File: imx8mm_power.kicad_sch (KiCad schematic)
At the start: 58 parts, among them U1 MIMX8MM6DVTLZAA

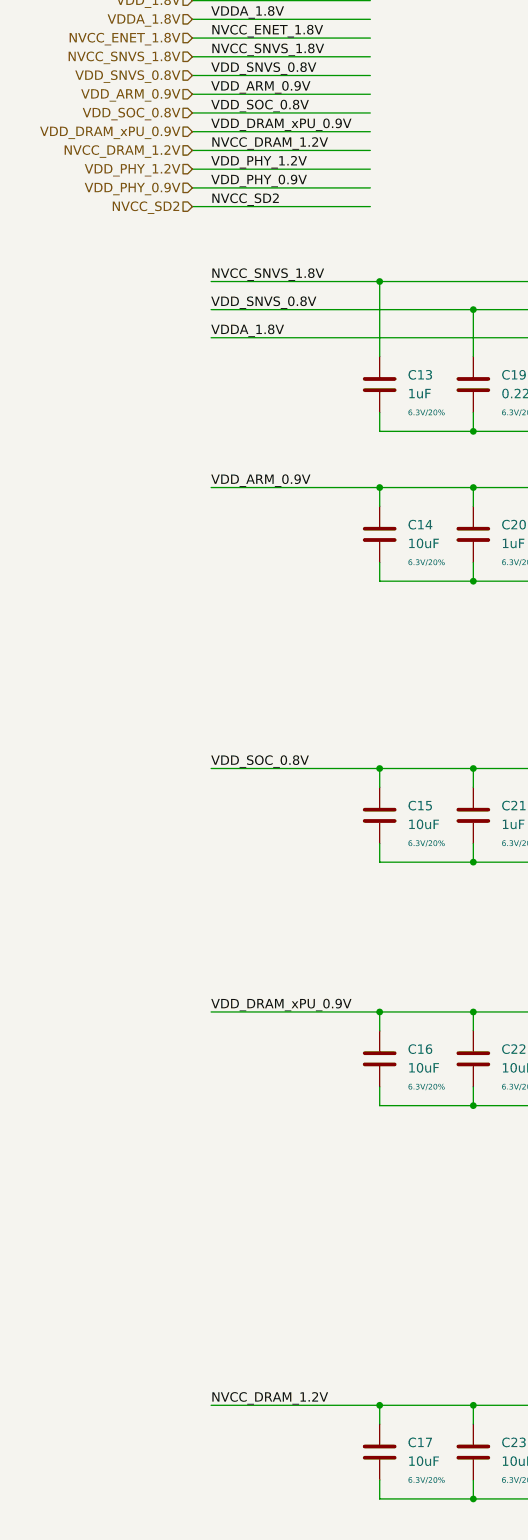
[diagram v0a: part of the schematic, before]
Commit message: add inital ddr tool version, lots of routing work
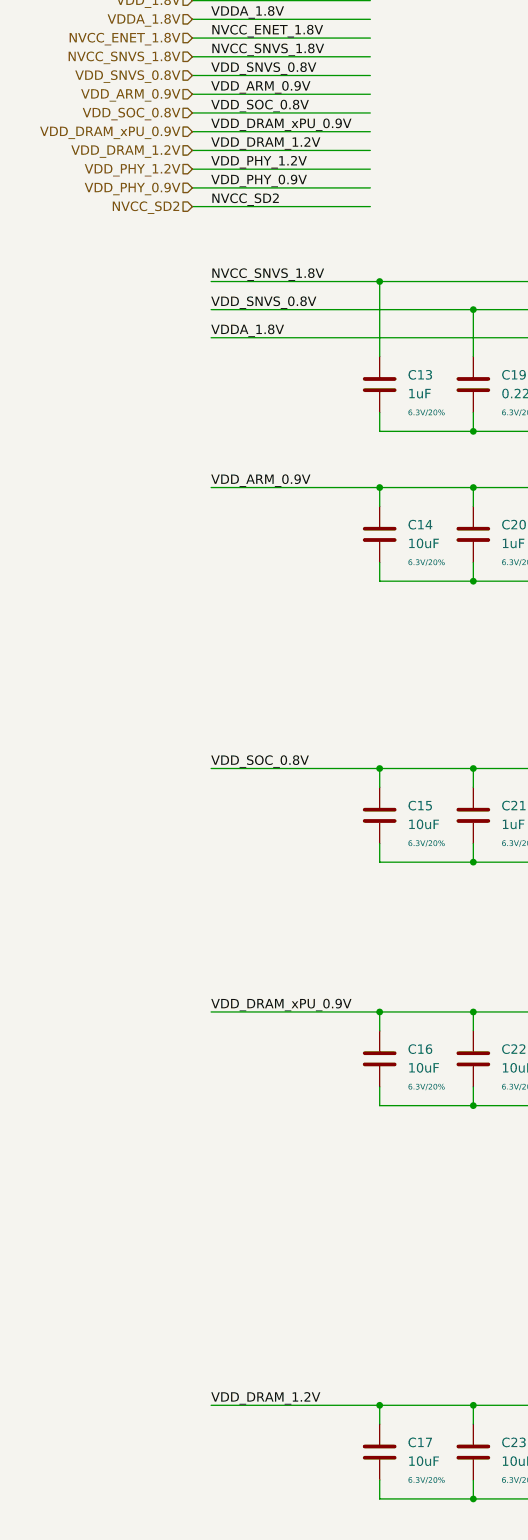
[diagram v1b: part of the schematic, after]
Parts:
- C13, C18, C19, C20, C21, C24, C25, C26, C27, C28, C29, C30, C31, C32, C33, C34, C35, C36, C37, C38, C39, C40, C41, C42, C43, C44, C45, C48, C49, C52, C54, C55, C56, C57, C58, C59, C60, C61, C62, C63, C64, C65, C66, C67, C68, C69: footprint Capacitor_SMD:C_0201_0603Metric -> qsbc:C_0201_0603Metric
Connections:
- net NVCC_DRAM_1.2V renamed VDD_DRAM_1.2V

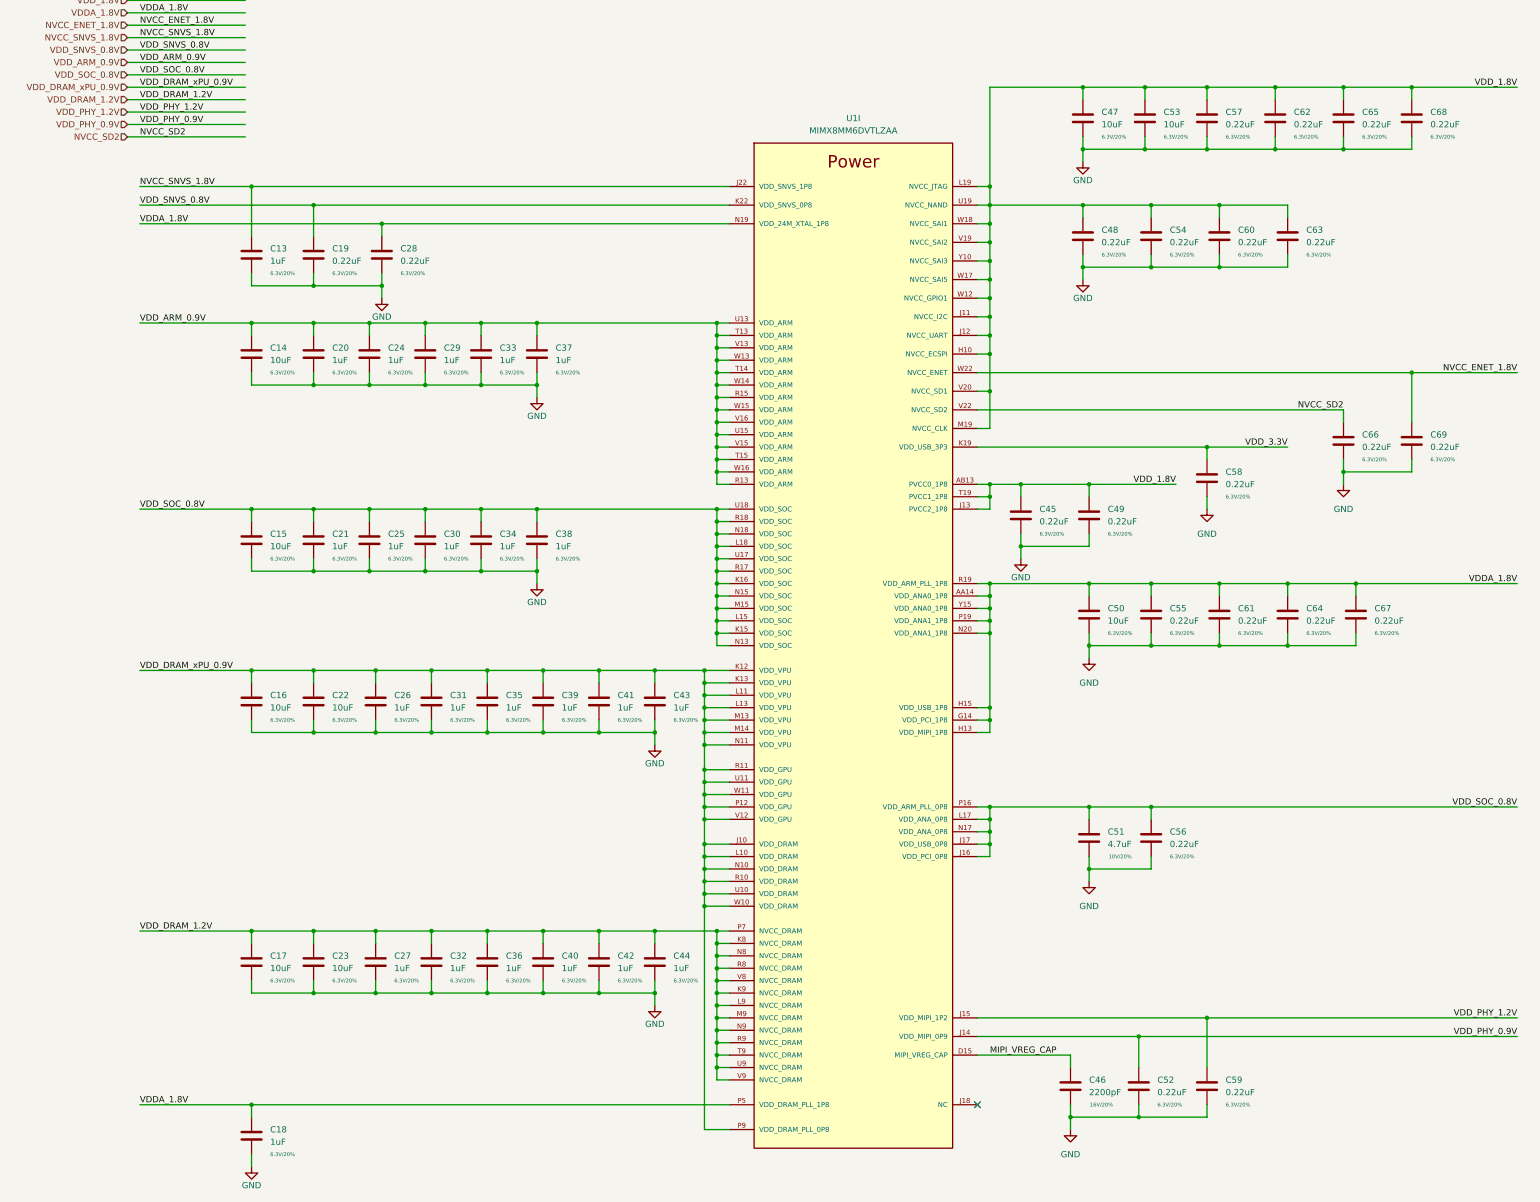
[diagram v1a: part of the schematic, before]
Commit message: inital routing of ddr data bus, sch work
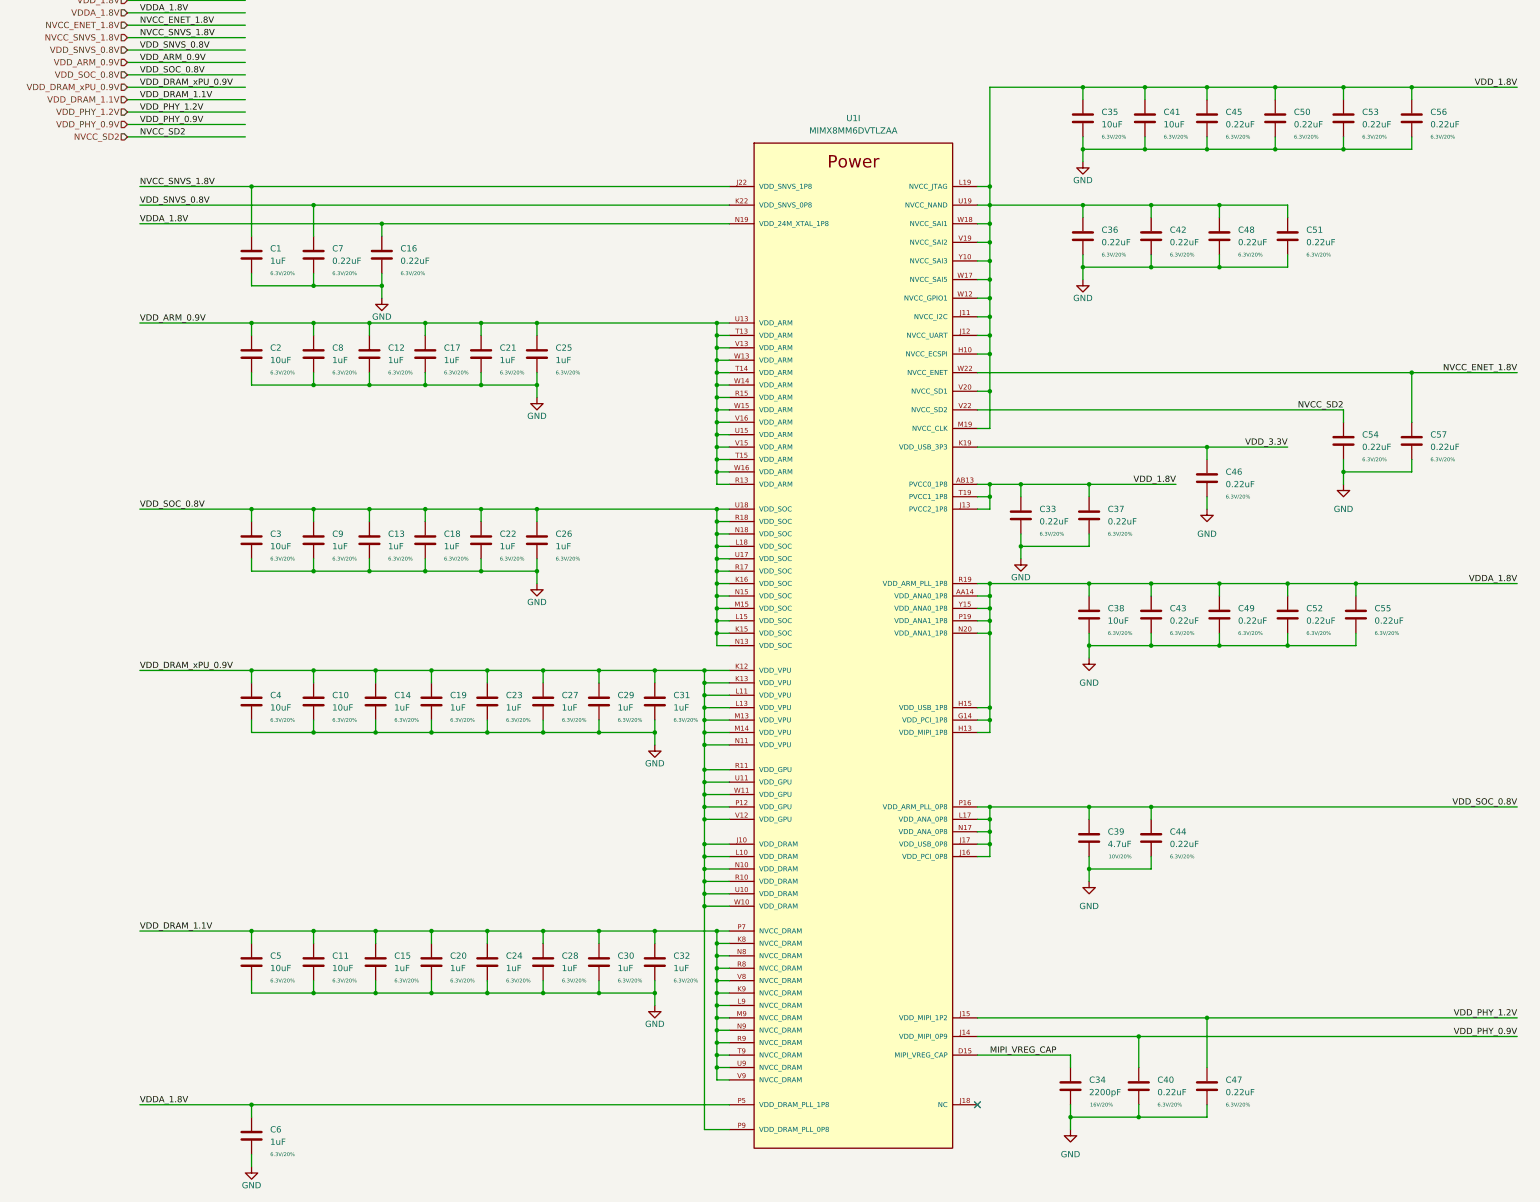
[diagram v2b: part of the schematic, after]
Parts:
- renumbered C13 to C1, C22 to C10, C23 to C11, C24 to C12, C25 to C13, C26 to C14, C27 to C15, C28 to C16, C29 to C17, C30 to C18, C31 to C19, C14 to C2, C32 to C20, C33 to C21, C34 to C22, C35 to C23, C36 to C24, C37 to C25, C38 to C26, C39 to C27, C40 to C28, C41 to C29, C15 to C3, C42 to C30, C43 to C31, C44 to C32, C45 to C33, C46 to C34, C47 to C35, C48 to C36, C49 to C37, C50 to C38, C51 to C39, C16 to C4, C52 to C40, C53 to C41, C54 to C42, C55 to C43, C56 to C44, C57 to C45, C58 to C46, C59 to C47, C60 to C48, C61 to C49, C17 to C5, C62 to C50, C63 to C51, C64 to C52, C65 to C53, C66 to C54, C67 to C55, C68 to C56, C69 to C57, C18 to C6, C19 to C7, C20 to C8, C21 to C9
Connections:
- net VDD_DRAM_1.2V renamed VDD_DRAM_1.1V

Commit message: add SN65DSI86 DSI2DP ic, SCH, PCB work, flytime work
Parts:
- C34: footprint Capacitor_SMD:C_0402_1005Metric -> qsbc:C_0201_0603Metric
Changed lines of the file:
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@@
       (effects (font (size 1.27 1.27)) (justify left))
     )
-    (property "Footprint" "Capacitor_SMD:C_0402_1005Metric" (id 2) (at 232.1052 251.46 0)
+    (property "Footprint" "qsbc:C_0201_0603Metric" (id 2) (at 232.1052 251.46 0)
       (effects (font (size 1.27 1.27)) hide)
     )

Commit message: change USB-UART conn, add new 0402 fp, more pcb work
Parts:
- C10, C11, C2, C3, C35, C38, C39, C4, C41, C5: footprint Capacitor_SMD:C_0402_1005Metric -> qsbc:C_0402_1005Metric
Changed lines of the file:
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@@
       (effects (font (size 1.27 1.27)) (justify left))
     )
-    (property "Footprint" "Capacitor_SMD:C_0402_1005Metric" (id 2) (at 77.1652 172.72 0)
+    (property "Footprint" "qsbc:C_0402_1005Metric" (id 2) (at 77.1652 172.72 0)
       (effects (font (size 1.27 1.27)) hide)
     )
@@
       (effects (font (size 1.27 1.27)) (justify left))
     )
-    (property "Footprint" "Capacitor_SMD:C_0402_1005Metric" (id 2) (at 64.4652 172.72 0)
+    (property "Footprint" "qsbc:C_0402_1005Metric" (id 2) (at 64.4652 172.72 0)
       (effects (font (size 1.27 1.27)) hide)
     )
@@
       (effects (font (size 1.27 1.27)) (justify left))
     )
-    (property "Footprint" "Capacitor_SMD:C_0402_1005Metric" (id 2) (at 77.1652 226.06 0)
+    (property "Footprint" "qsbc:C_0402_1005Metric" (id 2) (at 77.1652 226.06 0)
       (effects (font (size 1.27 1.27)) hide)
     )
@@
       (effects (font (size 1.27 1.27)) (justify left))
     )
-    (property "Footprint" "Capacitor_SMD:C_0402_1005Metric" (id 2) (at 247.3452 53.34 0)
+    (property "Footprint" "qsbc:C_0402_1005Metric" (id 2) (at 247.3452 53.34 0)
       (effects (font (size 1.27 1.27)) hide)
     )
@@
       (effects (font (size 1.27 1.27)) (justify left))
     )
-    (property "Footprint" "Capacitor_SMD:C_0402_1005Metric" (id 2) (at 64.4652 226.06 0)
+    (property "Footprint" "qsbc:C_0402_1005Metric" (id 2) (at 64.4652 226.06 0)
       (effects (font (size 1.27 1.27)) hide)
     )
@@
       (effects (font (size 1.27 1.27)) (justify left))
     )
-    (property "Footprint" "Capacitor_SMD:C_0402_1005Metric" (id 2) (at 235.9152 154.94 0)
+    (property "Footprint" "qsbc:C_0402_1005Metric" (id 2) (at 235.9152 154.94 0)
       (effects (font (size 1.27 1.27)) hide)
     )
@@
       (effects (font (size 1.27 1.27)) (justify left))
     )
-    (property "Footprint" "Capacitor_SMD:C_0402_1005Metric" (id 2) (at 64.4652 139.7 0)
+    (property "Footprint" "qsbc:C_0402_1005Metric" (id 2) (at 64.4652 139.7 0)
       (effects (font (size 1.27 1.27)) hide)
     )
@@
       (effects (font (size 1.27 1.27)) (justify left))
     )
-    (property "Footprint" "Capacitor_SMD:C_0402_1005Metric" (id 2) (at 235.9152 200.66 0)
+    (property "Footprint" "qsbc:C_0402_1005Metric" (id 2) (at 235.9152 200.66 0)
       (effects (font (size 1.27 1.27)) hide)
     )
@@
       (effects (font (size 1.27 1.27)) (justify left))
     )
-    (property "Footprint" "Capacitor_SMD:C_0402_1005Metric" (id 2) (at 64.4652 101.6 0)
+    (property "Footprint" "qsbc:C_0402_1005Metric" (id 2) (at 64.4652 101.6 0)
       (effects (font (size 1.27 1.27)) hide)
     )
@@
       (effects (font (size 1.27 1.27)) (justify left))
     )
-    (property "Footprint" "Capacitor_SMD:C_0402_1005Metric" (id 2) (at 234.6452 53.34 0)
-      (effects (font (size 1.27 1.27)) hide)
-    )
+    (property "Footprint" "qsbc:C_0402_1005Metric" (id 2) (at 234.6452 53.34 0)
+      (effects (font (size 1.27 1.27)) hide)
+    )
